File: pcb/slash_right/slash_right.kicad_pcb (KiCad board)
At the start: 2 copper layers, 137 parts, among them J1 RJ12, J2 AVR-ISP-6, J3 USB_B_Mini, SW1 SW_Push, SW10 SW_Push_45deg, SW11 SW_Push_45deg, SW12 SW_Push_45deg, SW13 SW_Push_45deg, SW14 SW_Push_45deg, SW15 SW_Push_45deg, SW16 SW_Push_45deg, SW17 SW_Push_45deg, SW18 SW_Push_45deg, SW19 SW_Push_45deg, SW2 SW_Push_45deg, SW20 SW_Push_45deg, SW21 SW_Push_45deg, SW22 SW_Push_45deg, SW23 SW_Push_45deg, SW24 SW_Push_45deg, SW25 SW_Push_45deg, SW26 SW_Push_45deg, SW27 SW_Push_45deg, SW28 SW_Push_45deg, SW29 SW_Push_45deg, SW3 SW_Push_45deg, SW30 SW_Push_45deg, SW31 SW_Push_45deg, SW32 SW_Push_45deg, SW33 SW_Push_45deg, SW34 SW_Push_45deg, SW35 SW_Push_45deg, SW36 SW_Push_45deg, SW37 SW_Push_45deg, SW38 SW_Push_45deg, SW39 SW_Push_45deg, SW4 SW_Push_45deg, SW40 SW_Push_45deg, SW41 SW_Push_45deg, SW42 SW_Push_45deg, SW43 SW_Push_45deg, SW44 SW_Push_45deg, SW45 SW_Push_45deg, SW46 SW_Push_45deg, SW47 SW_Push_45deg, SW48 SW_Push_45deg, SW49 SW_Push_45deg, SW5 SW_Push_45deg, SW50 SW_Push_45deg, SW51 SW_Push_45deg, SW52 SW_Push_45deg, SW53 SW_Push_45deg, SW54 SW_Push_45deg, SW55 SW_Push_45deg, SW56 SW_Push_45deg, SW6 SW_Push_45deg, SW7 SW_Push_45deg, SW8 SW_Push_45deg, SW9 SW_Push_45deg, U1 ATmega32U4-AU, Y1 16MHz

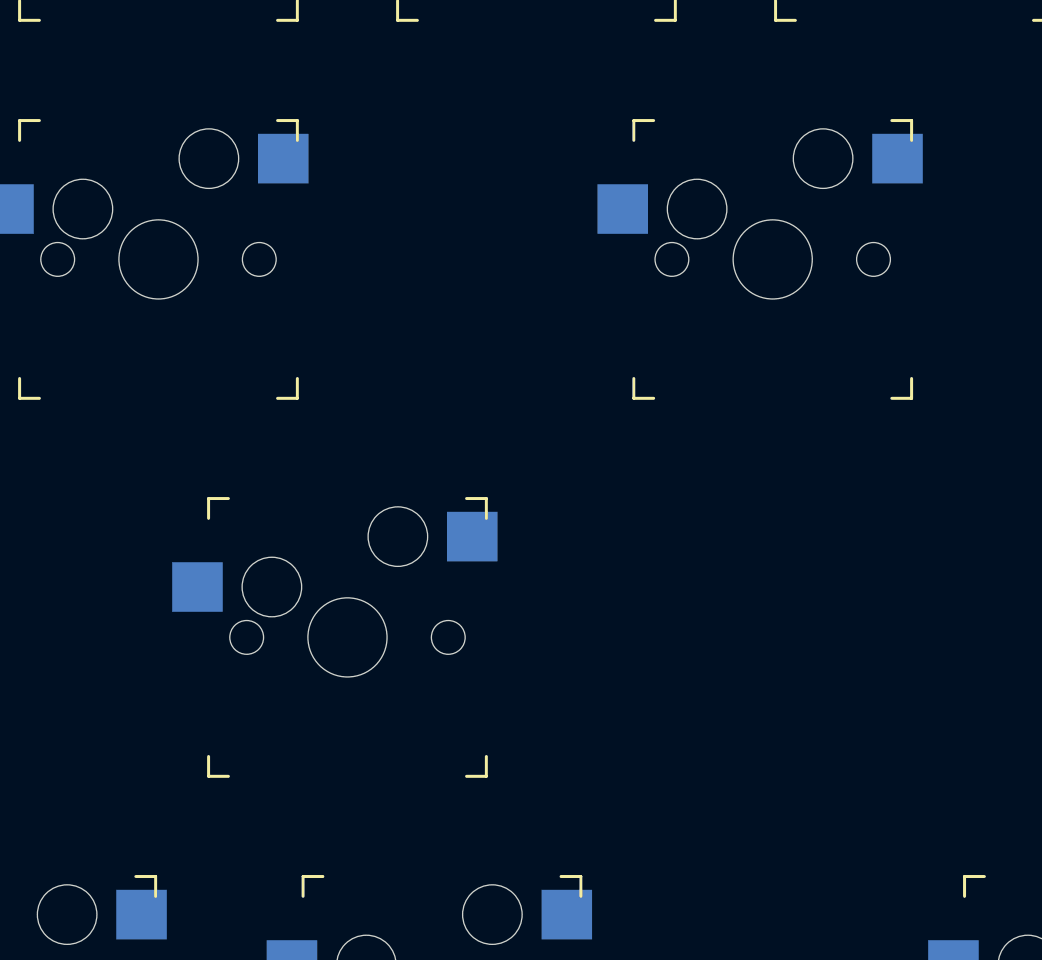
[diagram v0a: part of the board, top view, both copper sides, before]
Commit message: pcb: slash_righ: Place switches
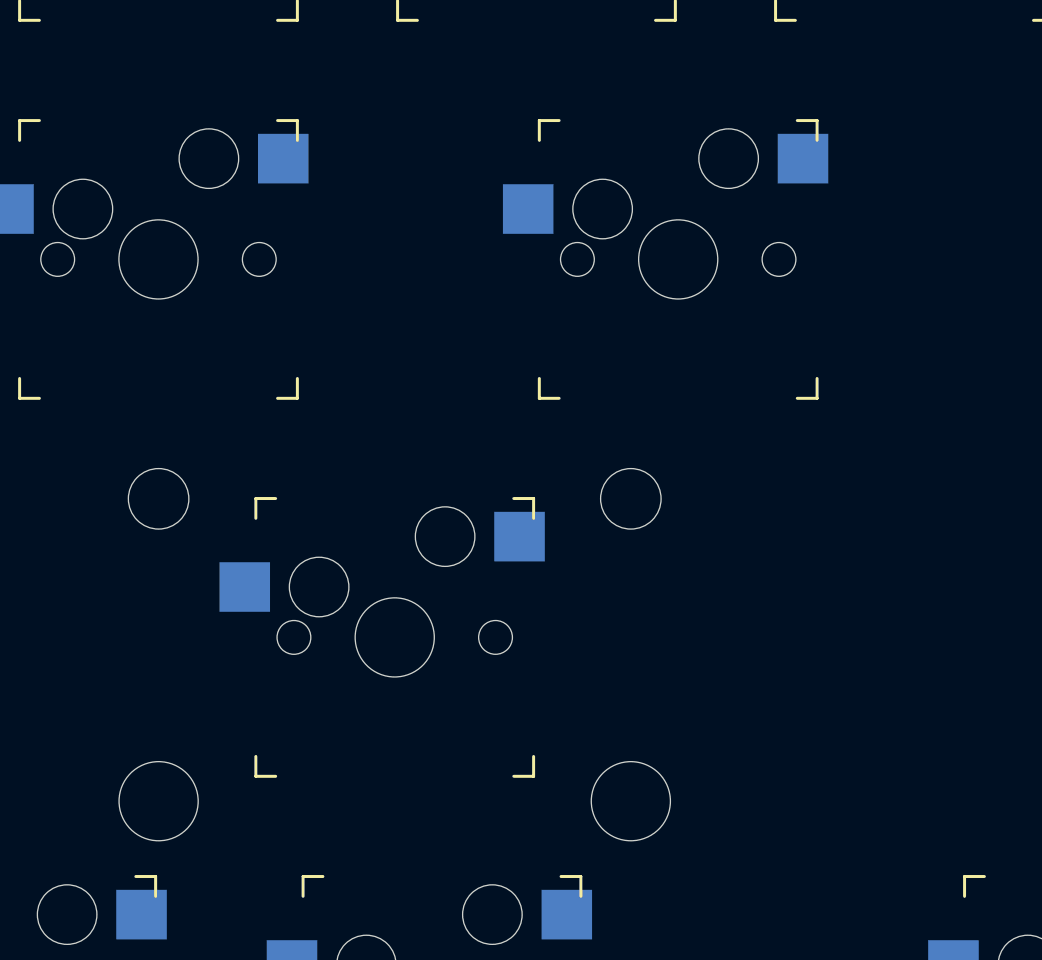
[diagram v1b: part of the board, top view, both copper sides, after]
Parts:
- added H1: MountingHole, keyswitches:Stabilizer_MX_2u, F.Cu at (145.3, 119.1)
- moved SW44 4.76 mm to (159.5, 100.0)
- moved SW39 2.38 mm to (145.3, 119.1)
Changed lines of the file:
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@@
     (tracks 0)
     (zones 0)
-    (modules 137)
+    (modules 138)
     (nets 98)
   )
@@
     (add_net "Net-(U1-Pad42)")
   )
+  (module keyswitches:Stabilizer_MX_2u (layer F.Cu)
+    (at 145.25625 119.0625)
+    (descr "MX-style stabilizer mount")
+    (tags MX,cherry,gateron,kailh,pg1511,stabilizer,stab)
+    (fp_text reference H1 (at 0 0) (layer F.Fab) hide
+      (effects (font (size 1 1) (thickness 0.15)))
+    )
+    (fp_text value MountingHole (at 0 10.16) (layer F.Fab) hide
+      (effects (font (size 1 1) (thickness 0.15)))
+    )
+    (fp_circle (center 0 0) (end 3 0) (layer Cmts.User) (width 0.15))
+    (pad "" np_thru_hole circle (at -11.9 -6.985) (size 3.048 3.048) (drill 3.048) (layers *.Cu *.Mask))
+    (pad "" np_thru_hole circle (at 11.9 -6.985) (size 3.048 3.048) (drill 3.048) (layers *.Cu *.Mask))
+    (pad "" np_thru_hole circle (at -11.9 8.255) (size 3.9878 3.9878) (drill 3.9878) (layers *.Cu *.Mask))
+    (pad "" np_thru_hole circle (at 11.9 8.255) (size 3.9878 3.9878) (drill 3.9878) (layers *.Cu *.Mask))
+  )
   (module Crystal:Crystal_HC49-U_Vertical (layer F.Cu)
     (at 301.21 106.54)
@@
   )
   (module keyswitches:Kailh_socket_MX (layer F.Cu)
-    (at 164.30625 100.0125)
+    (at 159.54375 100.0125)
     (descr "MX-style keyswitch with Kailh socket mount")
     (tags MX,cherry,gateron,kailh,pg1511,socket)
@@
   )
   (module keyswitches:Kailh_socket_MX (layer F.Cu)
-    (at 142.875 119.0625)
-    (descr "MX-style keyswitch with Kailh socket mount")
-    (tags MX,cherry,gateron,kailh,pg1511,socket)
+    (at 145.25625 119.0625)
+    (descr "MX-style keyswitch with Kailh socket mount")
+    (tags MX,cherry,gateron,kailh,pg1511,socket)

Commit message: pcb: slash_right: rough layout
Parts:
- C1, C2, C3, C4, C5, C6, C7, C8, C9, D1, D10, D11, D12, D13, D14, D15, D16, D17, D18, D19, D2, D20, D21, D22, D23, D24, D25, D26, D27, D28, D29, D3, D30, D31, D32, D33, D34, D35, D36, D37, D38, D39, D40, D41, D42, D43, D44, D45, D46, D47, D48, D49, D5, D50, D51, D52, D53, D54, D55, D56, D57, D58, D59, D6, D7, D8, D9, F1, R1, R2, R3, R4, R5, R6, R7, U1, Y1: moved to B.Cu
- moved J1 456.6 mm to (22.8, 45.6), turned to 270 degrees
- moved D2 432.6 mm to (14.2, 60.0)
- moved R5 430.4 mm to (21.8, 65.4)
- moved D19 424.1 mm to (64.3, 142.9), turned to 90 degrees
- moved D13 422.4 mm to (45.2, 142.9), turned to 90 degrees
- moved D9 418.7 mm to (64.3, 66.7), turned to 90 degrees
- moved D1 411.0 mm to (29.2, 43.1)
- moved D11 397.2 mm to (45.2, 104.8), turned to 90 degrees
- moved D16 395.8 mm to (83.3, 85.7), turned to 90 degrees
- moved D24 387.0 mm to (83.3, 123.8), turned to 90 degrees
- moved D25 377.5 mm to (90.5, 142.9), turned to 90 degrees
- moved D4 366.1 mm to (21.7, 62.5)
- moved D17 359.2 mm to (64.3, 104.8), turned to 90 degrees
- moved D12 359.2 mm to (45.2, 123.8), turned to 90 degrees
- moved D23 358.9 mm to (83.3, 104.8), turned to 90 degrees
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
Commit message: pcb: slash: right: Start routing
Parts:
- moved C3 40.8 mm to (210.9, 112.2), turned to 225 degrees
- moved C2 38.3 mm to (214.4, 115.7), turned to 45 degrees
- moved Y1 35.2 mm to (210.5, 119.6), turned to 135 degrees
- moved D4 33.5 mm to (39.1, 33.8), turned to 90 degrees
- moved C5 30.2 mm to (195.8, 138.7), turned to 180 degrees
- moved C4 27.8 mm to (187.1, 112.3), turned to 90 degrees
- moved C6 27.0 mm to (188.5, 130.7), turned to 270 degrees
- moved D21 26.8 mm to (128.2, 73.8)
- moved D22 26.8 mm to (128.2, 92.9)
- moved D26 26.8 mm to (152.0, 50.0)
- moved SW24 26.8 mm to (140.1, 69.1)
- moved SW33 26.8 mm to (140.1, 126.2)
- moved D29 26.8 mm to (128.2, 111.9)
- moved D30 26.8 mm to (128.2, 131.0)
- moved SW25 26.8 mm to (140.1, 88.1)
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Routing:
- net /ROW0: track 0.00 -> 362.0 mm
- net /ROW2: track 0.00 -> 295.3 mm
- net /ROW1: track 0.00 -> 292.0 mm
- net /COL9: track 0.00 -> 53.6 mm, vias 0 -> 3
- net /COL10: track 0.00 -> 38.1 mm
- net GND: track 0.00 -> 34.4 mm
- net +5V: track 0.00 -> 31.6 mm
- net /D1-: track 0.00 -> 20.9 mm
- net /D1+: track 0.00 -> 17.0 mm
- net Net-(C4-Pad1): track 0.00 -> 16.9 mm, vias 0 -> 2
- net Net-(C2-Pad1): track 0.00 -> 12.2 mm
- net Net-(C3-Pad2): track 0.00 -> 12.2 mm
- net Net-(D41-Pad2): track 0.00 -> 8.55 mm
- net Net-(D29-Pad2): track 0.00 -> 8.55 mm
- net Net-(D48-Pad2): track 0.00 -> 8.55 mm
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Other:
- board outline added: 218 x 127 mm
- net class Default: trace_width 0.25 -> 0.4
- net class Power added: clearance 0.2, trace_width 0.5, via_dia 0.8, via_drill 0.4

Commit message: pcb: slash: right: Continue
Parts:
- D3: moved to F.Cu
- J2: moved to B.Cu
- moved C1 33.5 mm to (188.8, 117.8)
- moved C6 27.6 mm to (213.4, 118.8), turned to 90 degrees
- moved R3 24.6 mm to (191.8, 133.0), turned to 270 degrees
- moved R2 21.2 mm to (187.6, 132.9), turned to 270 degrees
- moved D47 18.9 mm to (173.6, 112.0)
- moved D3 14.1 mm to (239.3, 126.7), turned to 90 degrees
- moved C2 12.6 mm to (205.7, 106.5), turned to 90 degrees
- moved C4 11.8 mm to (189.3, 123.9), turned to 270 degrees
- moved C3 11.6 mm to (200.8, 106.6), turned to 270 degrees
- moved R1 10.6 mm to (239.3, 126.7), turned to 90 degrees
- moved Y1 9.21 mm to (205.7, 111.8), turned to 180 degrees
- moved J2 8.53 mm to (248.6, 128.2), turned to 180 degrees
- moved C9 7.59 mm to (194.2, 111.8), turned to 90 degrees
- moved D42 6.05 mm to (182.8, 127.0)
- moved C5 5.60 mm to (198.3, 133.7), turned to 0 degrees
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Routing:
- net /D-: track 0.00 -> 183.3 mm
- net /D+: track 0.00 -> 180.0 mm
- net /SDA: track 0.00 -> 70.8 mm
- net /SCL: track 0.00 -> 69.5 mm
- net Net-(D47-Pad2): track 8.55 -> 29.1 mm
- net /~RST: track 0.00 -> 19.6 mm
- net +5V: track 31.6 -> 44.0 mm
- net /D1-: track 20.9 -> 9.57 mm
- net /ROW2: track 295.3 -> 287.9 mm, vias 0 -> 6
- net /ROW1: track 292.0 -> 298.4 mm, vias 0 -> 6
- net GND: track 34.4 -> 39.8 mm, vias 0 -> 5
- net Net-(C4-Pad1): track 16.9 -> 12.4 mm
- net /D1+: track 17.0 -> 12.9 mm
- net Net-(D42-Pad2): track 8.55 -> 7.15 mm
- net Net-(D7-Pad2): track 8.55 -> 9.50 mm
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- added copper zone on F.Cu, net GND

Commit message: pcb: slash: Progress
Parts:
- moved R5 160.3 mm to (190.6, 144.9)
- moved D2 60.3 mm to (99.3, 55.7), turned to 180 degrees
- moved F1 23.6 mm to (53.1, 33.8), turned to 90 degrees
- moved D1 7.68 mm to (62.7, 50.5), turned to 90 degrees
- moved R7 5.21 mm to (118.1, 54.7), turned to 270 degrees
- moved R6 3.43 mm to (123.6, 54.6), turned to 270 degrees
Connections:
- J2 pad 1: /COL3 -> /COL18
- J2 pad 3: /COL1 -> /COL16
- J2 pad 4: /COL2 -> /COL17
- U1 pad 10: /COL2 -> /COL17
- U1 pad 11: /COL3 -> /COL18
- U1 pad 39: /COL18 -> /COL3
- U1 pad 40: /COL17 -> /COL2
- U1 pad 41: /COL16 -> /COL1
- U1 pad 9: /COL1 -> /COL16
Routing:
- net +5V: track 44.0 -> 368.4 mm
- net /SCL: track 69.5 -> 243.6 mm, vias 0 -> 6
- net /SDA: track 70.8 -> 241.6 mm, vias 0 -> 2
- net /D-: track 183.3 -> 235.9 mm, vias 0 -> 2
- net /D+: track 180.0 -> 217.9 mm
- net /~RST: track 19.6 -> 31.7 mm
- net /ROW2: track 287.9 -> 280.1 mm
- net /ROW1: track 298.4 -> 290.8 mm
- net Net-(F1-Pad2): track 0.00 -> 7.13 mm
- net GND: track 39.8 -> 41.6 mm, vias 5 -> 6

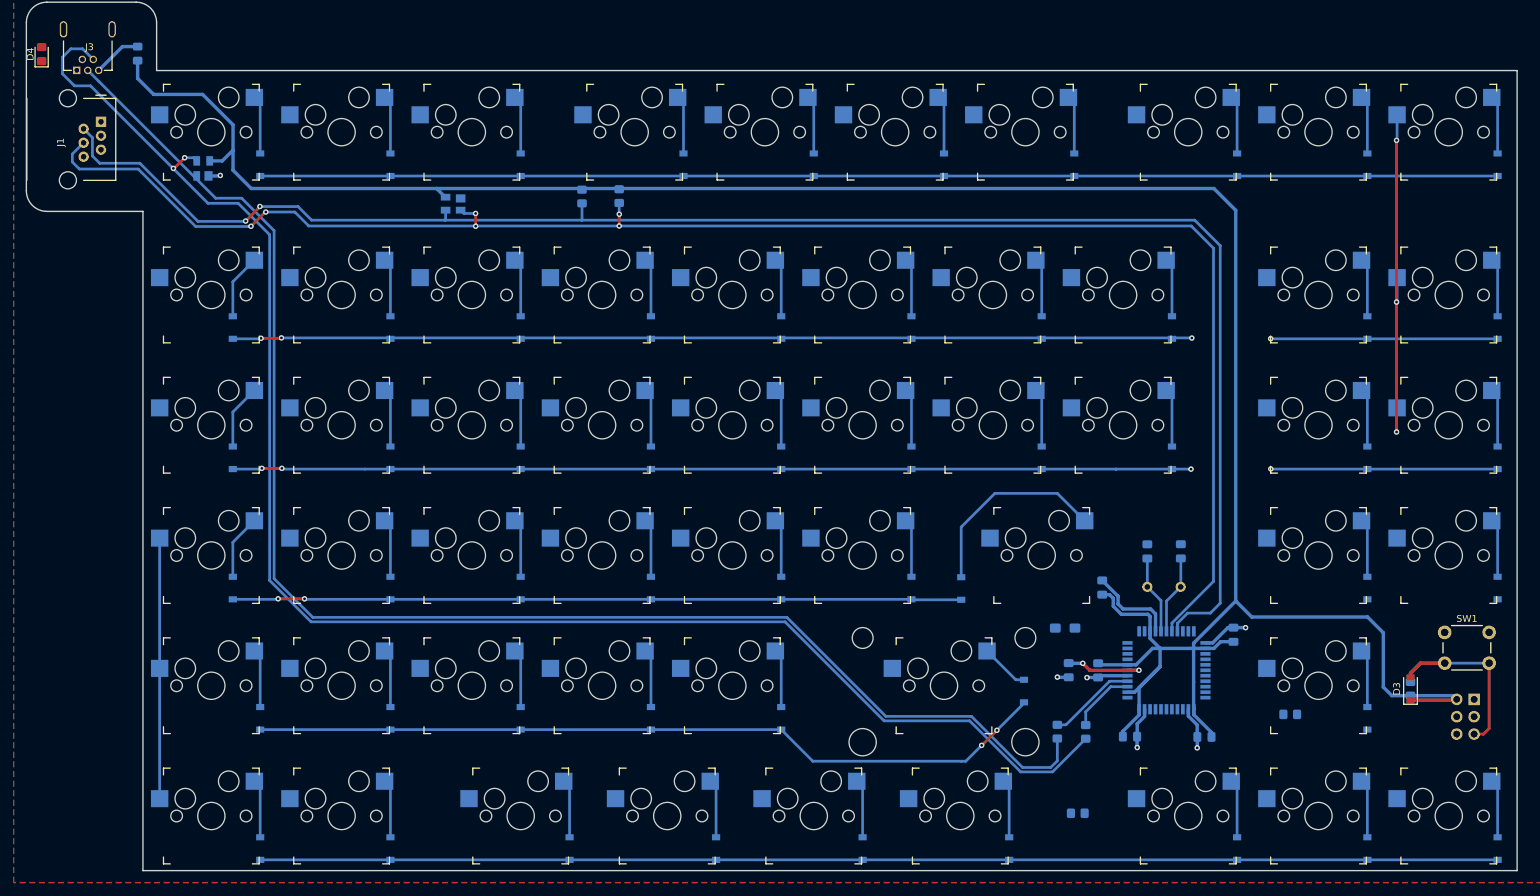
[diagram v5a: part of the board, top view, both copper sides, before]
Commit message: pcb: slash: more routing
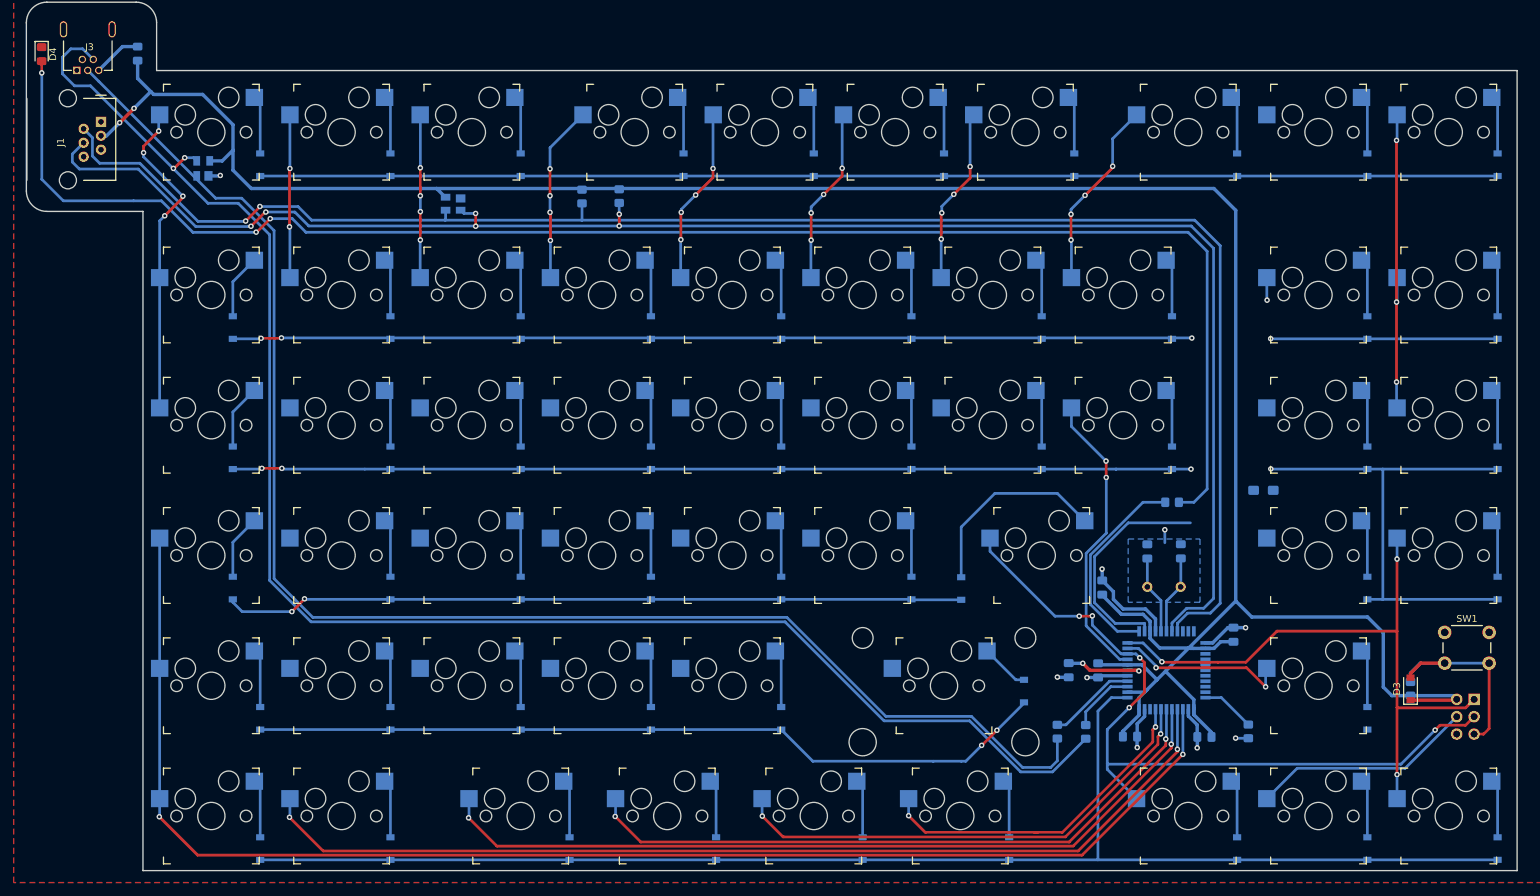
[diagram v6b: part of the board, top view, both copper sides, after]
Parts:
- moved R5 47.5 mm to (204.4, 99.4)
- moved C1 35.3 mm to (217.8, 97.6)
- moved R4 6.62 mm to (215.6, 132.9), turned to 90 degrees
- turned D4 to 270 degrees
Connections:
- U1 pad 1: Net-(R5-Pad1) -> /ROW0
- U1 pad 12: /COL7 -> Net-(R5-Pad1)
- U1 pad 20: /COL10 -> Net-(U1-Pad20)
- U1 pad 21: /COL11 -> Net-(U1-Pad21)
- U1 pad 22: /COL13 -> Net-(U1-Pad22)
- U1 pad 25: /COL12 -> Net-(U1-Pad25)
- U1 pad 26: /COL14 -> Net-(U1-Pad26)
- U1 pad 27: /COL15 -> Net-(U1-Pad27)
- U1 pad 36: /ROW2 -> /COL10
- U1 pad 37: /ROW1 -> /COL11
- U1 pad 38: /ROW0 -> /COL12
- U1 pad 39: /COL3 -> /COL13
- U1 pad 40: /COL2 -> /COL14
- U1 pad 41: /COL1 -> /COL15
- U1 pad 8: /COL0 -> /COL7
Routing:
- net Net-(D4-Pad2): track 0.00 -> 233.4 mm, vias 0 -> 3
- net /COL10: track 38.1 -> 205.5 mm, vias 0 -> 2
- net /COL11: track 0.00 -> 146.9 mm, vias 0 -> 2
- net /COL12: track 0.00 -> 119.0 mm, vias 0 -> 2
- net /COL16: track 0.00 -> 112.6 mm, vias 0 -> 5
- net /COL13: track 0.00 -> 95.9 mm, vias 0 -> 2
- net /COL18: track 0.00 -> 92.4 mm, vias 0 -> 3
- net /COL14: track 0.00 -> 72.6 mm, vias 0 -> 2
- net /COL7: track 0.00 -> 71.1 mm, vias 0 -> 6
- net /COL17: track 0.00 -> 58.2 mm, vias 0 -> 2
- net /COL15: track 0.00 -> 50.0 mm, vias 0 -> 2
- net /COL0: track 0.00 -> 47.6 mm, vias 0 -> 4
- net /ROW2: track 280.1 -> 319.9 mm
- net /~RST: track 31.7 -> 64.3 mm
- net Net-(R5-Pad1): track 0.00 -> 30.3 mm
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- added copper zone on B.Cu, net GND
